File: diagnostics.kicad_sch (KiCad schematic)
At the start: 2 parts

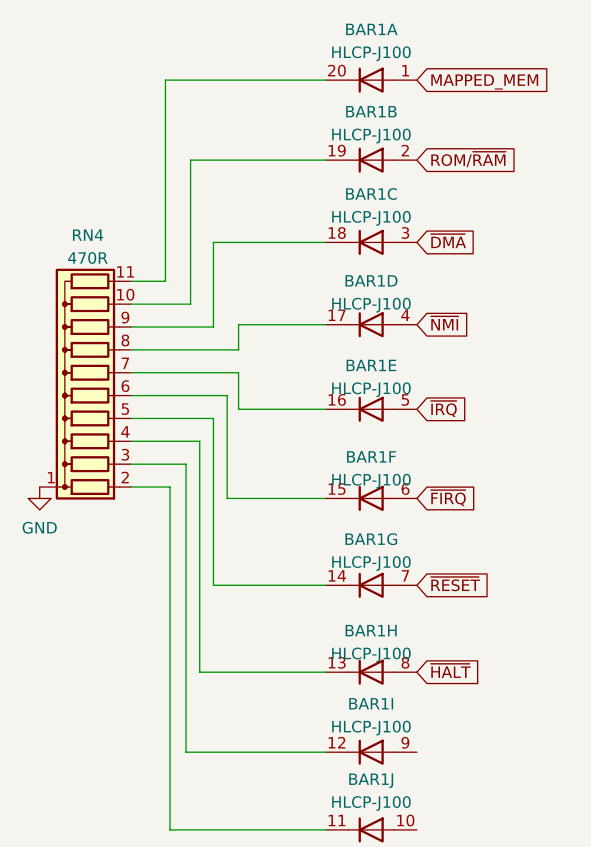
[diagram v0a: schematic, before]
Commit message: use 10 segment led bar
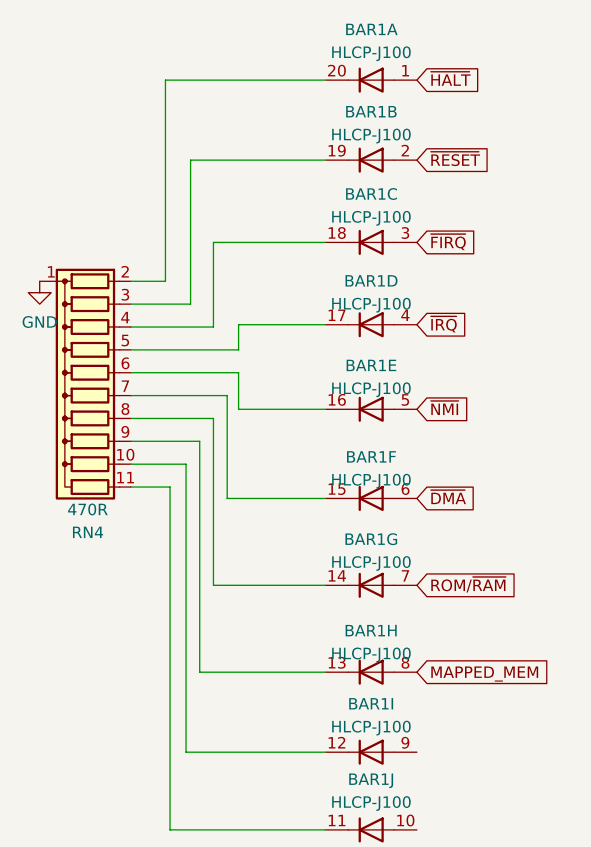
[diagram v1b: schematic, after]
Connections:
- net MAPPED_MEM: now also BAR1.8 (A); no longer BAR1.1 (A)
- net ROM/~{RAM}: now also BAR1.7 (A); no longer BAR1.2 (A)
- net ~{DMA}: now also BAR1.6 (A); no longer BAR1.3 (A)
- net ~{FIRQ}: now also BAR1.3 (A); no longer BAR1.6 (A)
- net ~{HALT}: now also BAR1.1 (A); no longer BAR1.8 (A)
- net ~{IRQ}: now also BAR1.4 (A); no longer BAR1.5 (A)
- net ~{NMI}: now also BAR1.5 (A); no longer BAR1.4 (A)
- net ~{RESET}: now also BAR1.2 (A); no longer BAR1.7 (A)
- net at BAR1.13 (K): now also RN4.9 (R8); no longer RN4.4 (R3)
- net at BAR1.16 (K): now also RN4.6 (R5); no longer RN4.7 (R6)
- net at BAR1.19 (K): now also RN4.3 (R2); no longer RN4.10 (R9)
- net at BAR1.20 (K): now also RN4.2 (R1); no longer RN4.11 (R10)
- net at BAR1.11 (K): now also RN4.11 (R10); no longer RN4.2 (R1)
- net at BAR1.12 (K): now also RN4.10 (R9); no longer RN4.3 (R2)
- net at RN4.5 (R4): now also BAR1.17 (K); no longer BAR1.14 (K)
- net at BAR1.15 (K): now also RN4.7 (R6); no longer RN4.6 (R5)
- net at RN4.8 (R7): now also BAR1.14 (K); no longer BAR1.17 (K)
- net at BAR1.18 (K): now also RN4.4 (R3); no longer RN4.9 (R8)

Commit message: tidy up component placing
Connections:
- net +5V: now reaches BAR1.10 (A)
- no-connect marks 0 -> 1
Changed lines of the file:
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@@
 (kicad_sch (version 20230121) (generator eeschema)
   (paper "A4")
+  (no_connect (at 148.844 113.792))
   (wire (pts (xy 138.684 85.598) (xy 127.762 85.598))
     (stroke (width 0) (type default))
@@
         )
       )
+    )
+  )
+  (symbol (lib_id "power:+5V") (at 148.844 122.428 270) (unit 1)
+    (in_bom yes) (on_board yes) (dnp no) (fields_autoplaced)
+    (property "Reference" "#PWR06" (at 145.034 122.428 0)
+      (effects (font (size 1.27 1.27)) hide)
+    )
+    (property "Value" "+5V" (at 152.4 123.063 90)
+      (effects (font (size 1.27 1.27)) (justify left))
+    )
+    (property "Footprint" "" (at 148.844 122.428 0)
+      (effects (font (size 1.27 1.27)) hide)
+    )
+    (property "Datasheet" "" (at 148.844 122.428 0)
+      (effects (font (size 1.27 1.27)) hide)
+    )
+    (pin "1")
+    (instances
+      (project "HD6309sbc"
+        (path "/b6976bcd-dc73-4942-aa19-f7adbf9104c7/d89ed66f-3f07-40a4-a82f-2642d873e0a8"
+          (reference "#PWR06") (unit 1)
+        )
+      )

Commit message: board refresh
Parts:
- removed RN4: 470R, Resistor_THT:R_Array_SIP11, symbol Device:R_Network10
- added RN4, RN5: 470R, Resistor_THT:R_Array_SIP6, symbol Device:R_Network05
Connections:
- net GND: now also RN4.1 (common), RN5.1 (common)
- net at BAR1.13 (K): now also RN5.4 (R3)
- net at BAR1.16 (K): now also RN4.6 (R5)
- net at BAR1.17 (K): now also RN4.5 (R4)
- net at BAR1.20 (K): now also RN4.2 (R1)
- net at BAR1.18 (K): now also RN4.4 (R3)
- net at BAR1.19 (K): now also RN4.3 (R2)
- net at BAR1.12 (K): now also RN5.3 (R2)
- net at BAR1.11 (K): now also RN5.2 (R1)
- net at BAR1.15 (K): now also RN5.6 (R5)
- net at BAR1.14 (K): now also RN5.5 (R4)
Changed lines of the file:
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@@
+    )
+  )
+  (symbol (lib_id "Device:R_Network05") (at 112.014 66.548 90) (mirror x) (unit 1)
+    (in_bom yes) (on_board yes) (dnp no) (fields_autoplaced)
+    (property "Reference" "RN4" (at 112.268 56.1848 90)
+      (effects (font (size 1.27 1.27)))
+    )
+    (property "Value" "470R" (at 112.268 58.7248 90)
+      (effects (font (size 1.27 1.27)))
+    )
+    (property "Footprint" "Resistor_THT:R_Array_SIP6" (at 112.014 76.073 90)
+      (effects (font (size 1.27 1.27)) hide)
+    )
+    (property "Datasheet" "http://www.vishay.com/docs/31509/csc.pdf" (at 112.014 66.548 0)
+      (effects (font (size 1.27 1.27)) hide)
+    )
+    (pin "1")
+    (pin "2")
+    (pin "3")
+    (pin "4")
+    (pin "5")
+    (pin "6")
+    (instances
+      (project "HD6309sbc"
+        (path "/b6976bcd-dc73-4942-aa19-f7adbf9104c7/d89ed66f-3f07-40a4-a82f-2642d873e0a8"
+          (reference "RN4") (unit 1)
+        )
+      )
+    )
+  )
+  (symbol (lib_id "power:GND") (at 106.934 84.328 270) (unit 1)
+    (in_bom yes) (on_board yes) (dnp no)
+    (property "Reference" "#PWR07" (at 100.584 84.328 0)
+      (effects (font (size 1.27 1.27)) hide)
+    )
+    (property "Value" "GND" (at 103.378 81.9404 90)
+      (effects (font (size 1.27 1.27)) (justify left))
+    )
+    (property "Footprint" "" (at 106.934 84.328 0)
+      (effects (font (size 1.27 1.27)) hide)
+    )
+    (property "Datasheet" "" (at 106.934 84.328 0)
+      (effects (font (size 1.27 1.27)) hide)
+    )
+    (pin "1")
+    (instances
+      (project "HD6309sbc"
+        (path "/b6976bcd-dc73-4942-aa19-f7adbf9104c7/d89ed66f-3f07-40a4-a82f-2642d873e0a8"
+          (reference "#PWR07") (unit 1)
+        )
+      )
     )
   )
@@
     )
   )
+  (symbol (lib_id "Device:R_Network05") (at 112.014 79.248 90) (unit 1)
+    (in_bom yes) (on_board yes) (dnp no)
+    (property "Reference" "RN5" (at 112.268 89.6112 90)
+      (effects (font (size 1.27 1.27)))
+    )
+    (property "Value" "470R" (at 112.268 87.0712 90)
+      (effects (font (size 1.27 1.27)))
+    )
+    (property "Footprint" "Resistor_THT:R_Array_SIP6" (at 112.014 69.723 90)
+      (effects (font (size 1.27 1.27)) hide)
+    )
+    (property "Datasheet" "http://www.vishay.com/docs/31509/csc.pdf" (at 112.014 79.248 0)
+      (effects (font (size 1.27 1.27)) hide)
+    )
+    (pin "1")
+    (pin "2")
+    (pin "3")
+    (pin "4")
+    (pin "5")
+    (pin "6")
+    (instances
+      (project "HD6309sbc"
+        (path "/b6976bcd-dc73-4942-aa19-f7adbf9104c7/d89ed66f-3f07-40a4-a82f-2642d873e0a8"
+          (reference "RN5") (unit 1)
+        )
+      )
+    )
+  )
   (symbol (lib_id "LED:HLCP-J100") (at 143.764 48.006 0) (mirror y) (unit 2)
     (in_bom yes) (on_board yes) (dnp no) (fields_autoplaced)
@@
     )
   )
-  (symbol (lib_id "Device:R_Network10") (at 112.014 74.168 90) (mirror x) (unit 1)
+  (symbol (lib_id "LED:HLCP-J100") (at 143.764 95.25 0) (mirror y) (unit 7)
+    (in_bom yes) (on_board yes) (dnp no) (fields_autoplaced)
+    (property "Reference" "BAR1" (at 143.764 90.17 0)
+      (effects (font (size 1.27 1.27)))
+    )
+    (property "Value" "HLCP-J100" (at 143.764 92.71 0)
+      (effects (font (size 1.27 1.27)))
+    )
+    (property "Footprint" "Display:HLCP-J100" (at 143.764 102.87 0)
+      (effects (font (size 1.27 1.27)) hide)
+    )
+    (property "Datasheet" "https://docs.broadcom.com/docs/AV02-1798EN" (at 143.764 95.25 0)
+      (effects (font (size 1.27 1.27)) hide)
+    )
+    (pin "1")
+    (pin "20")
+    (pin "19")
+    (pin "2")
+    (pin "18")
+    (pin "3")
+    (pin "17")
+    (pin "4")
+    (pin "16")
+    (pin "5")
+    (pin "15")
+    (pin "6")
+    (pin "14")
+    (pin "7")
+    (pin "13")
+    (pin "8")
+    (pin "12")
+    (pin "9")
+    (pin "10")
+    (pin "11")
+    (instances
+      (project "HD6309sbc"
+        (path "/b6976bcd-dc73-4942-aa19-f7adbf9104c7/d89ed66f-3f07-40a4-a82f-2642d873e0a8"
+          (reference "BAR1") (unit 7)
+        )
+      )
+    )
+  )
+  (symbol (lib_id "LED:HLCP-J100") (at 143.764 113.792 0) (mirror y) (unit 9)
+    (in_bom yes) (on_board yes) (dnp no) (fields_autoplaced)
+    (property "Reference" "BAR1" (at 143.764 108.458 0)
+      (effects (font (size 1.27 1.27)))
+    )
+    (property "Value" "HLCP-J100" (at 143.764 110.998 0)
+      (effects (font (size 1.27 1.27)))
+    )
+    (property "Footprint" "Display:HLCP-J100" (at 143.764 121.412 0)
+      (effects (font (size 1.27 1.27)) hide)
+    )
+    (property "Datasheet" "https://docs.broadcom.com/docs/AV02-1798EN" (at 143.764 113.792 0)
+      (effects (font (size 1.27 1.27)) hide)
+    )
+    (pin "1")
+    (pin "20")
+    (pin "19")
+    (pin "2")
+    (pin "18")
+    (pin "3")
+    (pin "17")
+    (pin "4")
+    (pin "16")
+    (pin "5")
+    (pin "15")
+    (pin "6")
+    (pin "14")
+    (pin "7")
+    (pin "13")
+    (pin "8")
+    (pin "12")
+    (pin "9")
+    (pin "10")
+    (pin "11")
+    (instances
+      (project "HD6309sbc"
+        (path "/b6976bcd-dc73-4942-aa19-f7adbf9104c7/d89ed66f-3f07-40a4-a82f-2642d873e0a8"
+          (reference "BAR1") (unit 9)
+        )
+      )
+    )
+  )
+  (symbol (lib_id "power:GND") (at 106.934 61.468 270) (unit 1)
     (in_bom yes) (on_board yes) (dnp no)
-    (property "Reference" "RN4" (at 112.268 89.408 90)
-      (effects (font (size 1.27 1.27)))
-    )
-    (property "Value" "470R" (at 112.268 86.868 90)
-      (effects (font (size 1.27 1.27)))
-    )
-    (property "Footprint" "Resistor_THT:R_Array_SIP11" (at 112.014 88.773 90)
-      (effects (font (size 1.27 1.27)) hide)
-    )
-    (property "Datasheet" "http://www.vishay.com/docs/31509/csc.pdf" (at 112.014 74.168 0)
-      (effects (font (size 1.27 1.27)) hide)
-    )
-    (pin "1")
-    (pin "10")
-    (pin "11")
-    (pin "2")
-    (pin "3")
-    (pin "4")
-    (pin "5")
-    (pin "6")
-    (pin "7")
-    (pin "8")
-    (pin "9")
-    (instances
-      (project "HD6309sbc"
-        (path "/b6976bcd-dc73-4942-aa19-f7adbf9104c7/d89ed66f-3f07-40a4-a82f-2642d873e0a8"
-          (reference "RN4") (unit 1)
-        )
-      )
-    )
-  )
-  (symbol (lib_id "LED:HLCP-J100") (at 143.764 95.25 0) (mirror y) (unit 7)
-    (in_bom yes) (on_board yes) (dnp no) (fields_autoplaced)
-    (property "Reference" "BAR1" (at 143.764 90.17 0)
-      (effects (font (size 1.27 1.27)))
-    )
-    (property "Value" "HLCP-J100" (at 143.764 92.71 0)
-      (effects (font (size 1.27 1.27)))
-    )
-    (property "Footprint" "Display:HLCP-J100" (at 143.764 102.87 0)
-      (effects (font (size 1.27 1.27)) hide)
-    )
-    (property "Datasheet" "https://docs.broadcom.com/docs/AV02-1798EN" (at 143.764 95.25 0)
-      (effects (font (size 1.27 1.27)) hide)
-    )
-    (pin "1")
-    (pin "20")
-    (pin "19")
-    (pin "2")
-    (pin "18")
-    (pin "3")
-    (pin "17")
-    (pin "4")
-    (pin "16")
-    (pin "5")
-    (pin "15")
-    (pin "6")
-    (pin "14")
-    (pin "7")
-    (pin "13")
-    (pin "8")
-    (pin "12")
-    (pin "9")
-    (pin "10")
-    (pin "11")
-    (instances
-      (project "HD6309sbc"
-        (path "/b6976bcd-dc73-4942-aa19-f7adbf9104c7/d89ed66f-3f07-40a4-a82f-2642d873e0a8"
-          (reference "BAR1") (unit 7)
-        )
-      )
-    )
-  )
-  (symbol (lib_id "LED:HLCP-J100") (at 143.764 113.792 0) (mirror y) (unit 9)
-    (in_bom yes) (on_board yes) (dnp no) (fields_autoplaced)
-    (property "Reference" "BAR1" (at 143.764 108.458 0)
-      (effects (font (size 1.27 1.27)))
-    )
-    (property "Value" "HLCP-J100" (at 143.764 110.998 0)
-      (effects (font (size 1.27 1.27)))
-    )
-    (property "Footprint" "Display:HLCP-J100" (at 143.764 121.412 0)
-      (effects (font (size 1.27 1.27)) hide)
-    )
-    (property "Datasheet" "https://docs.broadcom.com/docs/AV02-1798EN" (at 143.764 113.792 0)
-      (effects (font (size 1.27 1.27)) hide)
-    )
-    (pin "1")
-    (pin "20")
-    (pin "19")
-    (pin "2")
-    (pin "18")
-    (pin "3")
-    (pin "17")
-    (pin "4")
-    (pin "16")
-    (pin "5")
-    (pin "15")
-    (pin "6")
-    (pin "14")
-    (pin "7")
-    (pin "13")
-    (pin "8")
-    (pin "12")
-    (pin "9")
-    (pin "10")
-    (pin "11")
-    (instances
-      (project "HD6309sbc"
-        (path "/b6976bcd-dc73-4942-aa19-f7adbf9104c7/d89ed66f-3f07-40a4-a82f-2642d873e0a8"
-          (reference "BAR1") (unit 9)
-        )
-      )
-    )
-  )
-  (symbol (lib_id "power:GND") (at 106.934 61.468 0) (unit 1)
-    (in_bom yes) (on_board yes) (dnp no) (fields_autoplaced)
-    (property "Reference" "#PWR05" (at 106.934 67.818 0)
-      (effects (font (size 1.27 1.27)) hide)
-    )
-    (property "Value" "GND" (at 106.934 66.04 0)
-      (effects (font (size 1.27 1.27)))
+    (property "Reference" "#PWR05" (at 100.584 61.468 0)
+      (effects (font (size 1.27 1.27)) hide)
+    )
+    (property "Value" "GND" (at 103.4796 64.1096 90)
+      (effects (font (size 1.27 1.27)) (justify left))
     )
     (property "Footprint" "" (at 106.934 61.468 0)

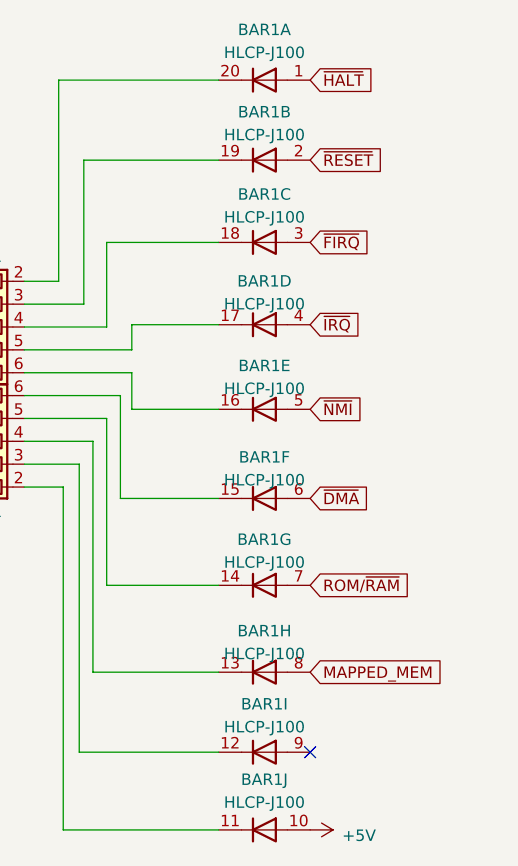
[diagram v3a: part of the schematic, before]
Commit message: Refine reset circuit
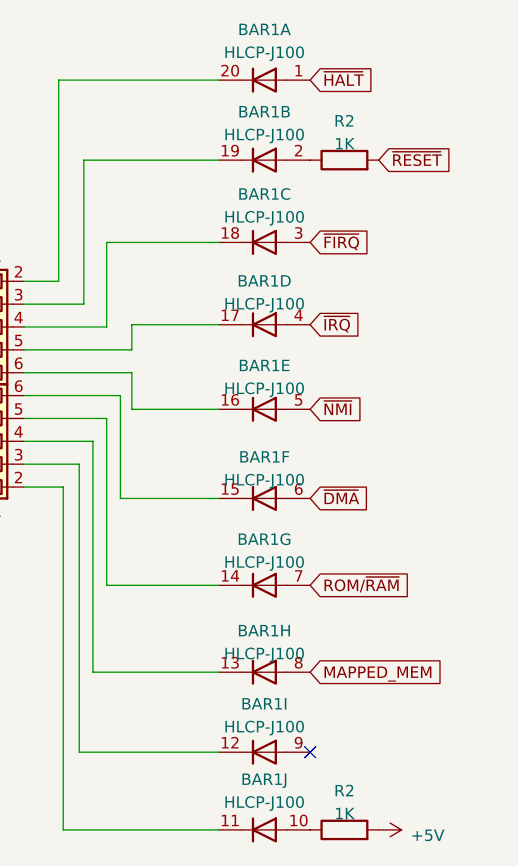
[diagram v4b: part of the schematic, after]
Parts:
- added R2 (x2): 1K, Resistor_SMD:R_0805_2012Metric_Pad1.20x1.40mm_HandSolder, symbol Device:R
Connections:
- net +5V: now also R2.2; no longer BAR1.10 (A)
- net ~{RESET}: now also R2.2; no longer BAR1.2 (A)
- new net: BAR1.2 (A), R2.1
- new net: BAR1.10 (A), R2.1
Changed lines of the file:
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@@
     )
   )
-  (global_label "~{RESET}" (shape input) (at 148.844 48.006 0) (fields_autoplaced)
+  (global_label "~{RESET}" (shape input) (at 156.464 48.006 0) (fields_autoplaced)
     (effects (font (size 1.27 1.27)) (justify left))
-    (property "Intersheetrefs" "${INTERSHEET_REFS}" (at 157.4949 48.006 0)
+    (property "Intersheetrefs" "${INTERSHEET_REFS}" (at 165.1149 48.006 0)
       (effects (font (size 1.27 1.27)) (justify left) hide)
     )
@@
     )
   )
+  (symbol (lib_id "Device:R") (at 152.654 122.428 90) (unit 1)
+    (in_bom yes) (on_board yes) (dnp no) (fields_autoplaced)
+    (property "Reference" "R2" (at 152.654 118.11 90)
+      (effects (font (size 1.27 1.27)))
+    )
+    (property "Value" "1K" (at 152.654 120.65 90)
+      (effects (font (size 1.27 1.27)))
+    )
+    (property "Footprint" "Resistor_SMD:R_0805_2012Metric_Pad1.20x1.40mm_HandSolder" (at 152.654 124.206 90)
+      (effects (font (size 1.27 1.27)) hide)
+    )
+    (property "Datasheet" "https://www.koaspeer.com/pdfs/RK73H.pdf" (at 152.654 122.428 0)
+      (effects (font (size 1.27 1.27)) hide)
+    )
+    (property "DigiKey" "" (at 152.654 122.428 0)
+      (effects (font (size 1.27 1.27)) hide)
+    )
+    (pin "1")
+    (pin "2")
+    (instances
+      (project "HD6309sbc"
+        (path "/b6976bcd-dc73-4942-aa19-f7adbf9104c7"
+          (reference "R2") (unit 1)
+        )
+        (path "/b6976bcd-dc73-4942-aa19-f7adbf9104c7/d89ed66f-3f07-40a4-a82f-2642d873e0a8"
+          (reference "R1") (unit 1)
+        )
+      )
+    )
+  )
+  (symbol (lib_id "power:+5V") (at 156.464 122.428 270) (unit 1)
+    (in_bom yes) (on_board yes) (dnp no) (fields_autoplaced)
+    (property "Reference" "#PWR06" (at 152.654 122.428 0)
+      (effects (font (size 1.27 1.27)) hide)
+    )
+    (property "Value" "+5V" (at 160.02 123.063 90)
+      (effects (font (size 1.27 1.27)) (justify left))
+    )
+    (property "Footprint" "" (at 156.464 122.428 0)
+      (effects (font (size 1.27 1.27)) hide)
+    )
+    (property "Datasheet" "" (at 156.464 122.428 0)
+      (effects (font (size 1.27 1.27)) hide)
+    )
+    (pin "1")
+    (instances
+      (project "HD6309sbc"
+        (path "/b6976bcd-dc73-4942-aa19-f7adbf9104c7/d89ed66f-3f07-40a4-a82f-2642d873e0a8"
+          (reference "#PWR06") (unit 1)
+        )
+      )
+    )
+  )
   (symbol (lib_id "LED:HLCP-J100") (at 143.764 95.25 0) (mirror y) (unit 7)
     (in_bom yes) (on_board yes) (dnp no) (fields_autoplaced)
@@
         (path "/b6976bcd-dc73-4942-aa19-f7adbf9104c7/d89ed66f-3f07-40a4-a82f-2642d873e0a8"
           (reference "BAR1") (unit 7)
+        )
+      )
+    )
+  )
+  (symbol (lib_id "Device:R") (at 152.654 48.006 90) (unit 1)
+    (in_bom yes) (on_board yes) (dnp no) (fields_autoplaced)
+    (property "Reference" "R2" (at 152.654 43.688 90)
+      (effects (font (size 1.27 1.27)))
+    )
+    (property "Value" "1K" (at 152.654 46.228 90)
+      (effects (font (size 1.27 1.27)))
+    )
+    (property "Footprint" "Resistor_SMD:R_0805_2012Metric_Pad1.20x1.40mm_HandSolder" (at 152.654 49.784 90)
+      (effects (font (size 1.27 1.27)) hide)
+    )
+    (property "Datasheet" "https://www.koaspeer.com/pdfs/RK73H.pdf" (at 152.654 48.006 0)
+      (effects (font (size 1.27 1.27)) hide)
+    )
+    (property "DigiKey" "" (at 152.654 48.006 0)
+      (effects (font (size 1.27 1.27)) hide)
+    )
+    (pin "1")
+    (pin "2")
+    (instances
+      (project "HD6309sbc"
+        (path "/b6976bcd-dc73-4942-aa19-f7adbf9104c7"
+          (reference "R2") (unit 1)
+        )
+        (path "/b6976bcd-dc73-4942-aa19-f7adbf9104c7/d89ed66f-3f07-40a4-a82f-2642d873e0a8"
+          (reference "R7") (unit 1)
         )
       )
@@
         )
       )
-    )
-  )
-  (symbol (lib_id "power:+5V") (at 148.844 122.428 270) (unit 1)
-    (in_bom yes) (on_board yes) (dnp no) (fields_autoplaced)
-    (property "Reference" "#PWR06" (at 145.034 122.428 0)
-      (effects (font (size 1.27 1.27)) hide)
-    )
-    (property "Value" "+5V" (at 152.4 123.063 90)
-      (effects (font (size 1.27 1.27)) (justify left))
-    )
-    (property "Footprint" "" (at 148.844 122.428 0)
-      (effects (font (size 1.27 1.27)) hide)
-    )
-    (property "Datasheet" "" (at 148.844 122.428 0)
-      (effects (font (size 1.27 1.27)) hide)
-    )
-    (pin "1")
-    (instances
-      (project "HD6309sbc"
-        (path "/b6976bcd-dc73-4942-aa19-f7adbf9104c7/d89ed66f-3f07-40a4-a82f-2642d873e0a8"
-          (reference "#PWR06") (unit 1)
-        )
-      )

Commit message: convert to new format
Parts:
- removed BAR1: HLCP-J100, Display:HLCP-J100, symbol LED:HLCP-J100
- removed R2 (x2): 1K, Resistor_SMD:R_0805_2012Metric_Pad1.20x1.40mm_HandSolder, symbol Device:R
- removed RN4, RN5: 470R, Resistor_THT:R_Array_SIP6, symbol Device:R_Network05
- added D10, D11, D12, D13, D14, D15, D16, D17, D4, D5, D6, D7, D8, D9: LED_Filled, LED_SMD:LED_1206_3216Metric_Pad1.42x1.75mm_HandSolder, symbol Device:LED_Filled
- added R1, R10, R11, R12, R13, R14, R15, R16, R17, R18, R19, R20, R21, R7: 470R, Resistor_SMD:R_0805_2012Metric_Pad1.20x1.40mm_HandSolder, symbol Device:R_Small
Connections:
- net GND: now also R1.2, R10.2, R11.2, R12.2, R13.2, R14.2, R15.2, R16.2, R17.2, R18.2, R19.2, R20.2, R21.2, R7.2
- net ~{FIRQ}: now also D14.2 (A)
- net ~{HALT}: now also D12.2 (A)
- net ~{IRQ}: now also D15.2 (A)
- net ~{NMI}: now also D16.2 (A)
- net ~{RESET}: now also D13.2 (A)
- new net: D13.1 (K), R17.1
- new net: D8.1 (K), R12.1
- new net: D14.1 (K), R18.1
- new net: D9.1 (K), R13.1
- new net: D12.1 (K), R16.1
- new net: D5.1 (K), R7.1
- new net: D16.1 (K), R20.1
- new net: D17.1 (K), R21.1
- new net: D10.1 (K), R14.1
- new net: D7.1 (K), R11.1
- new net: D11.1 (K), R15.1
- new net: D15.1 (K), R19.1
- new net: D4.1 (K), R1.1
- new net: D6.1 (K), R10.1
- new net BUSY: D17.2 (A)
- new net intD0: D4.2 (A)
- new net intD1: D5.2 (A)
- new net intD2: D6.2 (A)
- new net intD3: D7.2 (A)
- new net intD4: D8.2 (A)
- new net intD5: D9.2 (A)
- new net intD6: D10.2 (A)
- new net intD7: D11.2 (A)
- no-connect marks 1 -> 0
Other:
- title: (none) -> HD6309 Homebrew SBC
